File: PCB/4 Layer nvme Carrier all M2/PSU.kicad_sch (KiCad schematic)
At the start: 187 parts, among them J5 Barrel_Jack_Switch, J79 Conn_01x02_Pin, J80 Conn_01x02_Pin, J81 USB_C_Receptacle_USB2.0_14P, J82 Conn_01x04, Q8 2N7002, SW1 SW_Push, SW2 SW_Push, U15 SY8253ADC, U16 SY8253ADC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

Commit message: first all-M.2 version
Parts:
- removed R116: 56K/1%, A_HDJ_Library:R_0402_1005Metric, symbol Device:R
- J81: value USB_C_Receptacle_USB2.0_14P -> USB_C_Receptacle_USB2.0_16P; symbol Connector:USB_C_Receptacle_USB2.0_14P -> Connector:USB_C_Receptacle_USB2.0_16P; LCSC Part # (none) -> C2988369; MPN (none) -> GT-USB-7010ASV
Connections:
- net +3V3d: now also C434.1, C435.2, C436.2, C437.1, C438.2, C439.2, L431.2, R431.2; no longer C444.1, C445.2, C446.2, C447.1, C448.2, C449.2, L441.2, R441.2
- net +3V3e: now also C444.1, C445.2, C446.2, C447.1, C448.2, C449.2, L441.2, R441.2; no longer C454.1, C455.2, C456.2, C457.1, C458.2, C459.2, L451.2, R451.2
- net +3V3f: now also C454.1, C455.2, C456.2, C457.1, C458.2, C459.2, L451.2, R451.2; no longer C464.1, C465.2, C466.2, C467.1, C468.2, C469.2, L461.2, R461.2
- net +3V3g: now also C464.1, C465.2, C466.2, C467.1, C468.2, C469.2, L461.2, R461.2; no longer C434.1, C435.2, C436.2, C437.1, C438.2, C439.2, L431.2, R431.2
- net +5V: now also J82.4 (Pin_4)
- net +5Va: no longer J82.4 (Pin_4)
- net GND: now also U80.9 (CFG1)
- net PWR_EN: now also U480.4 (EN); no longer JP78.1 (A)
- net at C159.2, R101.1, U80.1 (VDD): now also U80.2 (CFG2), U80.3 (CFG3)
- net at JP78.2 (B): no longer U480.4 (EN)
- no-connect marks 0 -> 3
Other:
- moved on the sheet: C431, C432, C433, C434, C435, C436, C437, C438, C439, C441, C442, C443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

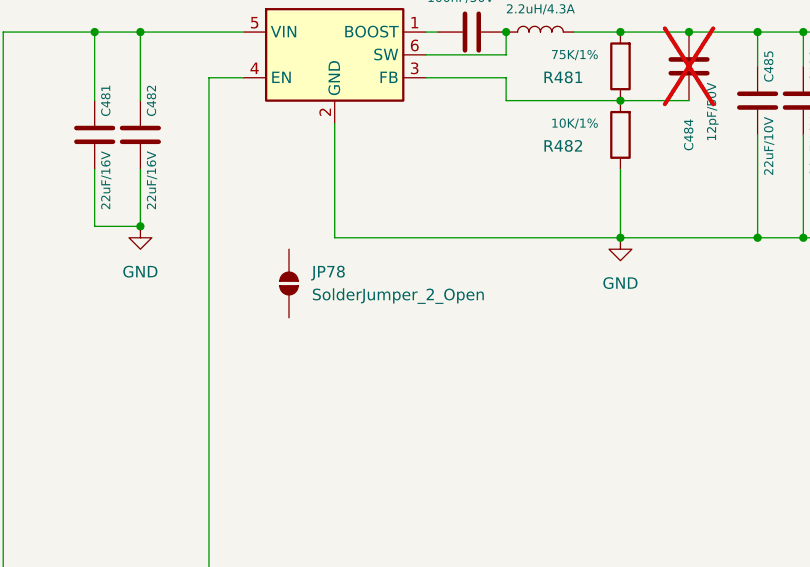
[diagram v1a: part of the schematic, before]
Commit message: Edit README for all-M.2 and add JPG
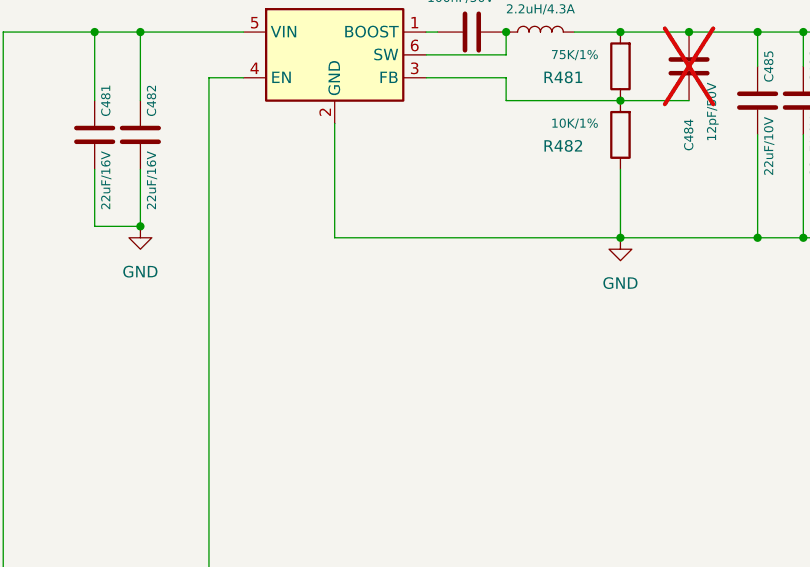
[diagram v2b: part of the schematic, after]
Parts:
- removed JP78: SolderJumper_2_Open, Jumper:SolderJumper-2_P1.3mm_Open_RoundedPad1.0x1.5mm, symbol Jumper:SolderJumper_2_Open
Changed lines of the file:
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@@
-	)
-	(symbol
-		(lib_id "Jumper:SolderJumper_2_Open")
-		(at 450.85 133.35 90)
-		(unit 1)
-		(exclude_from_sim no)
-		(in_bom yes)
-		(on_board yes)
-		(dnp no)
-		(fields_autoplaced yes)
-		(property "Reference" "JP78"
-			(at 453.39 132.0799 90)
-			(effects
-				(font
-					(size 1.27 1.27)
-				)
-				(justify right)
-			)
-		)
-		(property "Value" "SolderJumper_2_Open"
-			(at 453.39 134.6199 90)
-			(effects
-				(font
-					(size 1.27 1.27)
-				)
-				(justify right)
-			)
-		)
-		(property "Footprint" "Jumper:SolderJumper-2_P1.3mm_Open_RoundedPad1.0x1.5mm"
-			(at 450.85 133.35 0)
-			(effects
-				(font
-					(size 1.27 1.27)
-				)
-				(hide yes)
-			)
-		)
-		(property "Datasheet" "~"
-			(at 450.85 133.35 0)
-			(effects
-				(font
-					(size 1.27 1.27)
-				)
-				(hide yes)
-			)
-		)
-		(property "Description" "Solder Jumper, 2-pole, open"
-			(at 450.85 133.35 0)
-			(effects
-				(font
-					(size 1.27 1.27)
-				)
-				(hide yes)
-			)
-		)
-		(property "Package" "SolderJumper"
-			(at 450.85 133.35 0)
-			(effects
-				(font
-					(size 1.27 1.27)
-				)
-				(hide yes)
-			)
-		)
-		(pin "2"
-		)
-		(pin "1"
-		)
-		(instances
-			(project "nvme Carrier for LattePanda Mu"
-				(path "/2a6d114a-7fd7-4207-b5f7-4ea9c34f36aa/b23aee49-27d1-466d-98e2-113ee657e42b"
-					(reference "JP78")
-					(unit 1)
-				)
-			)
-		)
 	)
 	(symbol
